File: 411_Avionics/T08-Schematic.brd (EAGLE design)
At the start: 41 parts, among them IC1 BQ24022, J1 USB-MICROB, J3 JST-PH-2-SMT-RA, U3 LSM9DS0, U5 LTC1998, U6 ATMEGA32U4-AU, X1 8MHz

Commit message: Finished board layout!!  Still have to create ground planes and add ground vias, but other than that it's all done.  Hooray!
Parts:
- moved C15 72.5 mm to (11.4, 6.33)
- moved C16 71.7 mm to (9.33, 6.35)
- moved U2 44.5 mm to (16.7, 6.99)
- moved R11 38.6 mm to (32.5, 11.2)
- moved R9 37.7 mm to (32.5, 15.2)
- moved C2 31.9 mm to (48.1, 3.25), turned to 270 degrees
- moved C5 28.2 mm to (48.1, 19.6), turned to 90 degrees
- moved LED1 25.3 mm to (41.1, 22.6), turned to 180 degrees
- moved U3 24.9 mm to (55.0, 18.8)
- moved R10 22.6 mm to (32.5, 13.2)
- moved C13 21.5 mm to (28.5, 19.9)
- moved R7 21.0 mm to (32.3, 22.4), turned to 0 degrees
- moved R6 19.2 mm to (36.8, 22.4), turned to 0 degrees
- moved C3 19.1 mm to (58.5, 21.9), turned to 270 degrees
- moved C6 18.3 mm to (50.2, 19.6), turned to 90 degrees
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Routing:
- net MOSI: track 0.00 -> 64.3 mm, vias 0 -> 3
- net MISO: track 0.00 -> 52.0 mm, vias 0 -> 3
- net VCC: track 46.5 -> 93.3 mm
- net XM_EN: track 0.00 -> 28.9 mm, vias 0 -> 2
- net GYR_EN: track 0.00 -> 26.7 mm, vias 0 -> 2
- net N$1: track 0.00 -> 21.7 mm, vias 0 -> 2
- net N$17: track 0.00 -> 18.6 mm, vias 0 -> 2
- net N$16: track 0.00 -> 18.4 mm, vias 0 -> 2
- net MEM_EN: track 0.00 -> 15.8 mm, vias 0 -> 2
- net N$19: track 0.00 -> 14.6 mm, vias 0 -> 2
- net RED_LED: track 0.00 -> 11.6 mm
- net N$5: track 7.88 -> 18.6 mm, vias 0 -> 2
- net VBUS1: track 4.59 -> 14.9 mm
- net N$8: track 0.00 -> 7.96 mm
- net GREEN_LED: track 0.00 -> 7.91 mm
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
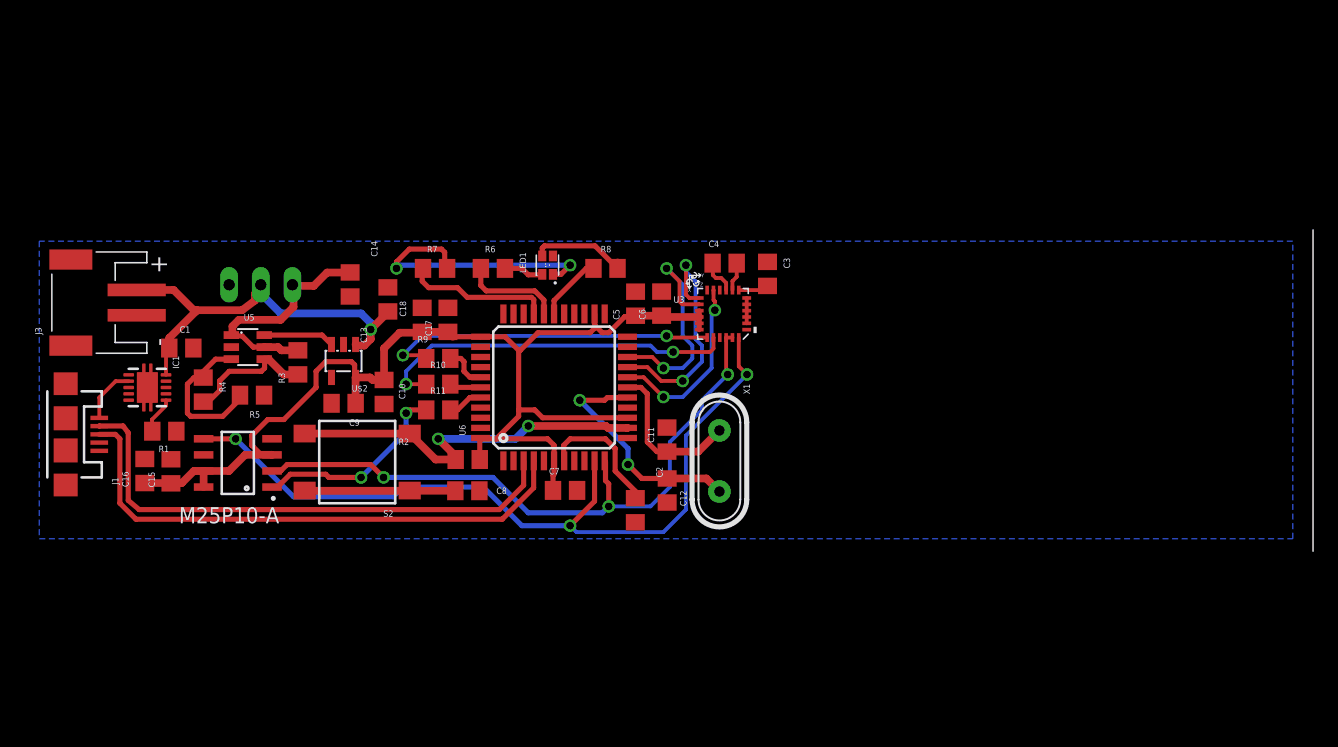
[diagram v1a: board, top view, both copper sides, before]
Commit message: More layout work.  All nodes connected, still need to run through DRC and deal with all that bs.
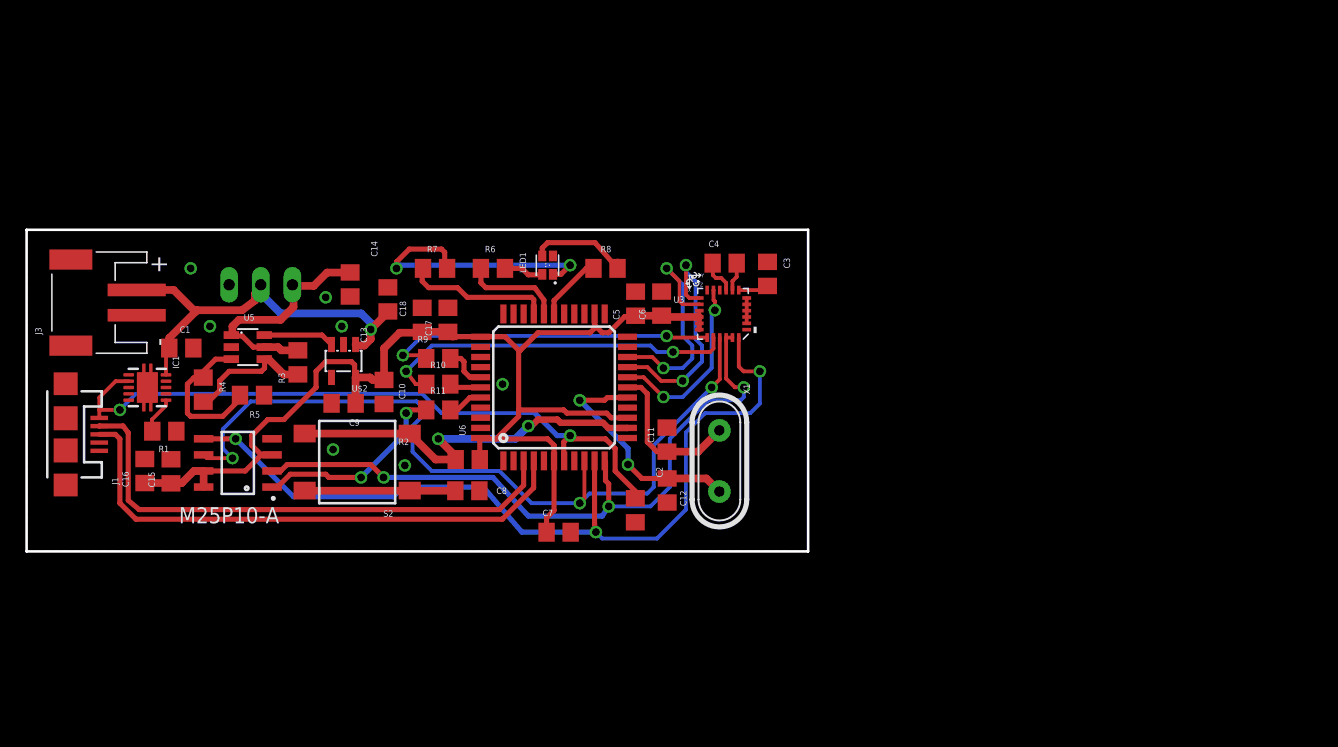
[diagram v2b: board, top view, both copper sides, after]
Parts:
- moved C7 3.34 mm to (42.0, 1.51)
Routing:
- net CLK: track 0.00 -> 64.4 mm, vias 0 -> 3
- net VBUS1: track 14.9 -> 54.3 mm, vias 0 -> 2
- net MOSI: track 64.3 -> 68.3 mm
- net MISO: track 52.0 -> 55.4 mm
- net VCC: track 93.3 -> 95.9 mm
- net XM_EN: track 28.9 -> 28.4 mm
- added copper zone on layer 1, net GND
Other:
- board outline added: 61.7 x 25.4 mm

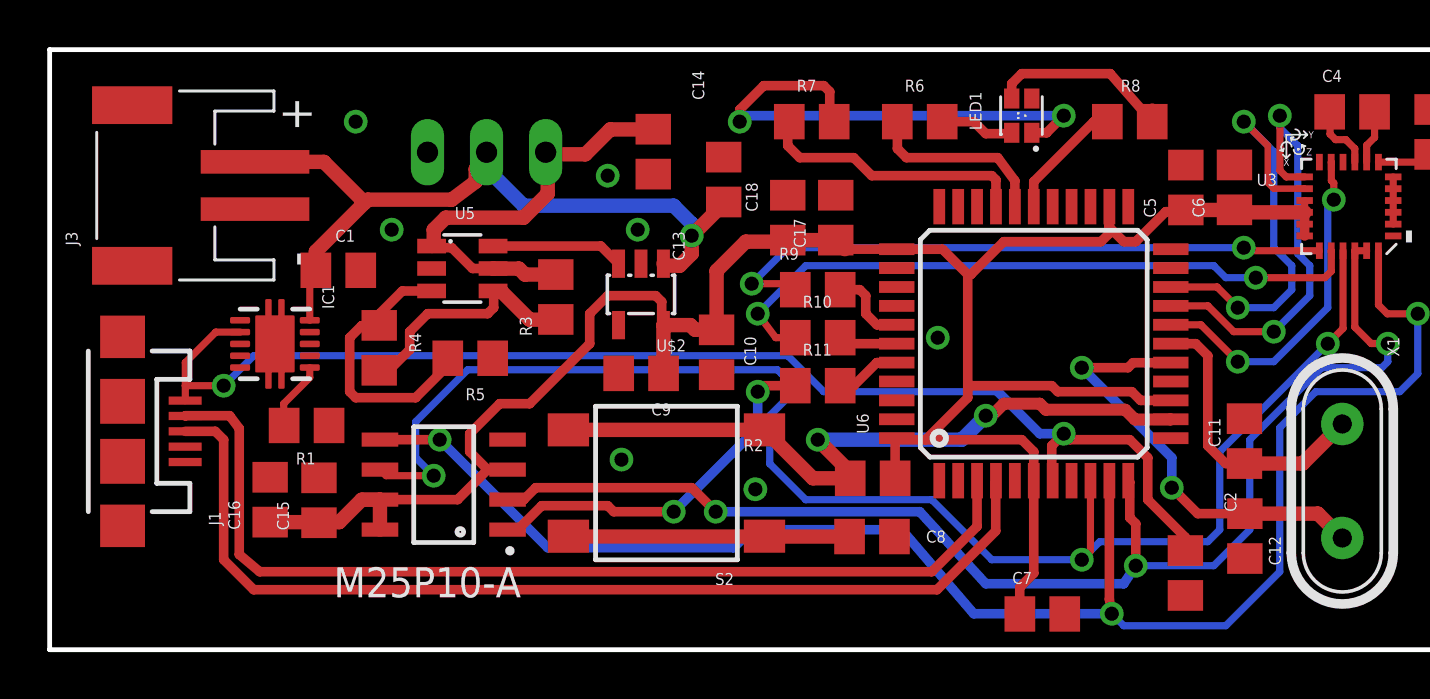
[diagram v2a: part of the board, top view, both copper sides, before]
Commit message: Made some changes to silkscreen layer, fixed package text size.
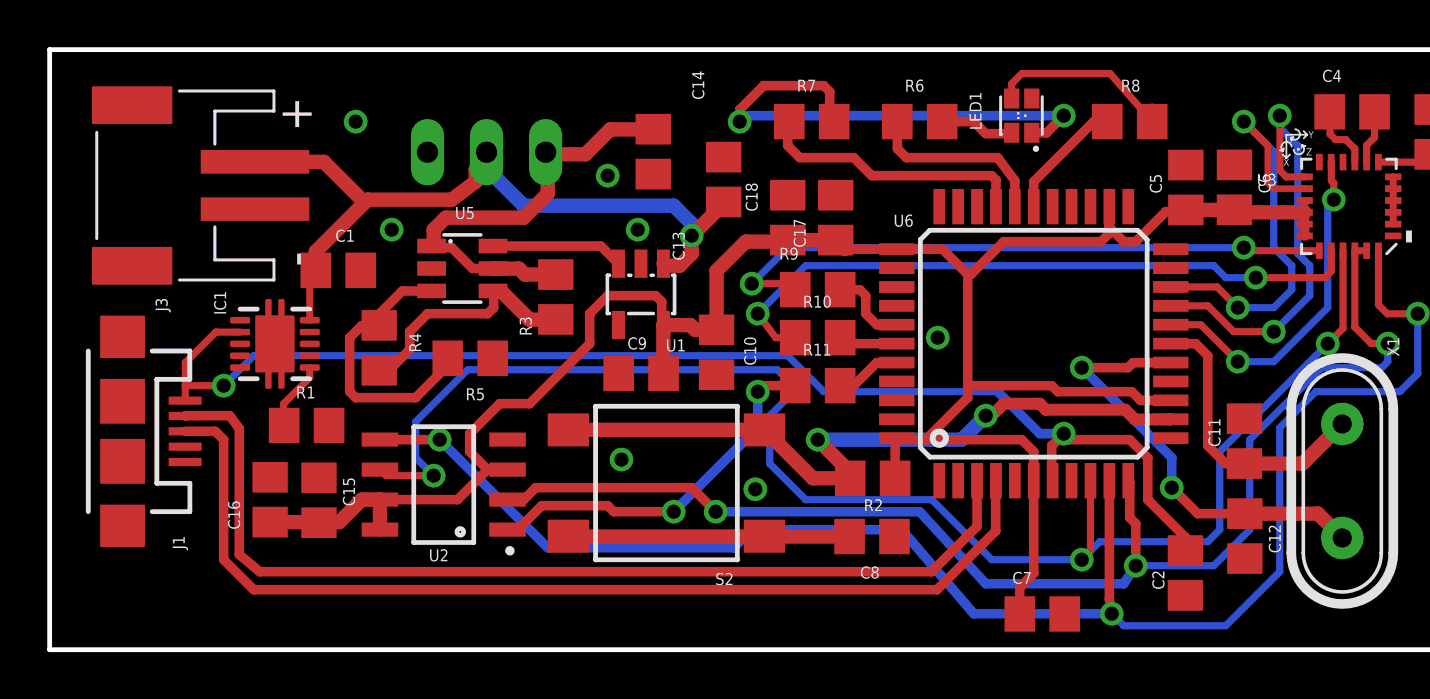
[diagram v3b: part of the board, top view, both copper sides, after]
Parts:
- U2: value (none) -> M25P10-AVMN6TP_TR
- renumbered U$2 to U1

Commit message: Finished preliminary board layout!  Passed OSHParks DRC, hooray!
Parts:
- moved C3 2.19 mm to (58.7, 19.7), turned to 90 degrees
- moved C7 0.64 mm to (41.6, 2.02)
- moved R4 0.51 mm to (14.5, 12.8)
- moved C15 0.51 mm to (11.4, 5.82)
- moved C16 0.51 mm to (9.33, 5.84)
- moved LED1 0.25 mm to (41.1, 22.4)
- moved R1 0.25 mm to (10.9, 9.75)
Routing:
- net GND: track 2.00 -> 6.91 mm, vias 0 -> 31
- net N$1: track 21.7 -> 19.5 mm, vias 2 -> 3
- net VCC: track 95.9 -> 97.1 mm
- net VBUS1: track 54.3 -> 55.3 mm, vias 2 -> 3
- net N$14: track 12.0 -> 11.0 mm
- net MOSI: track 68.3 -> 67.5 mm
- net BLUE_LED: track 5.22 -> 5.97 mm
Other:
- board text added: "Team 8, TinyAV"

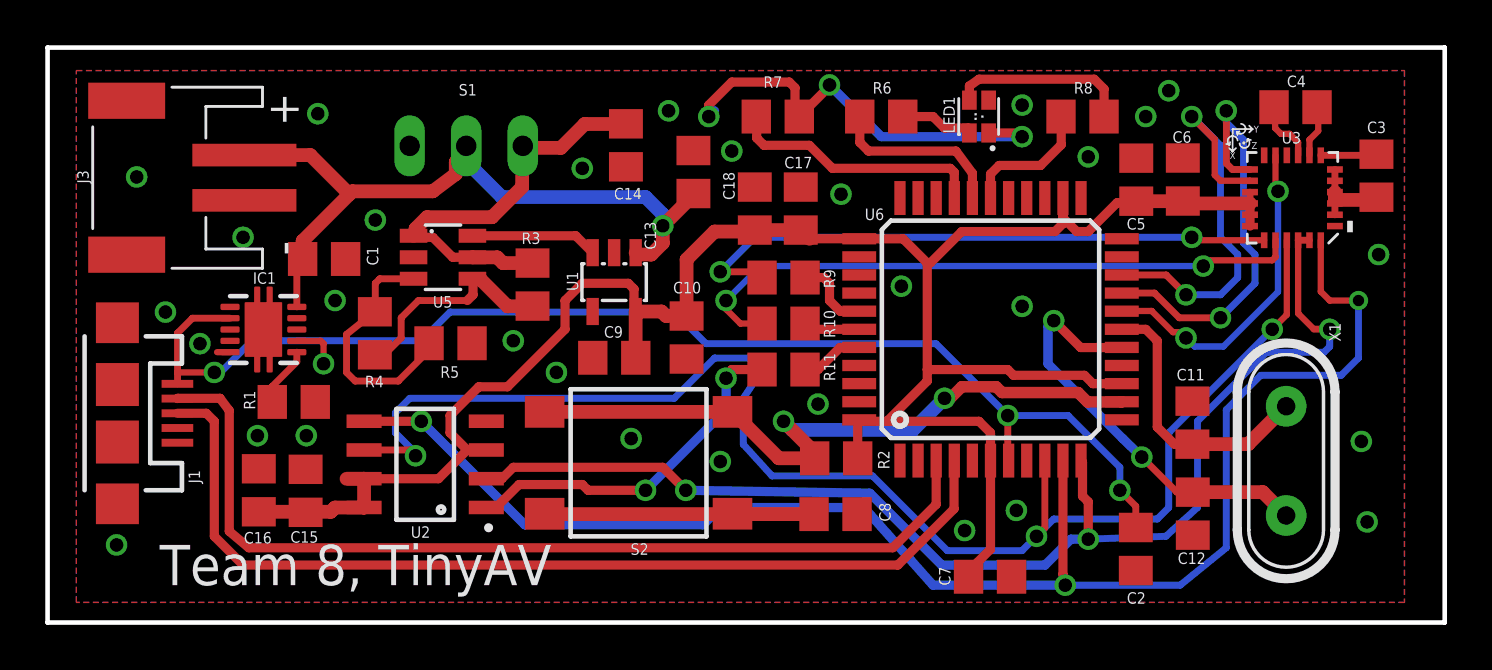
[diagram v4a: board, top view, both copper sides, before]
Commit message: Layout Review #1 With Andrew:
-changed all 0805 packages to 0603  (made a lot more room)
-made vias significantly smaller (made a lot more room)
-updated layout to reflect these changes, no DRC issues

We should consider hooking up the status pins of our battery charger to
LEDs.  Should also consider increasing the value of our current limiting
resistors from the processor.
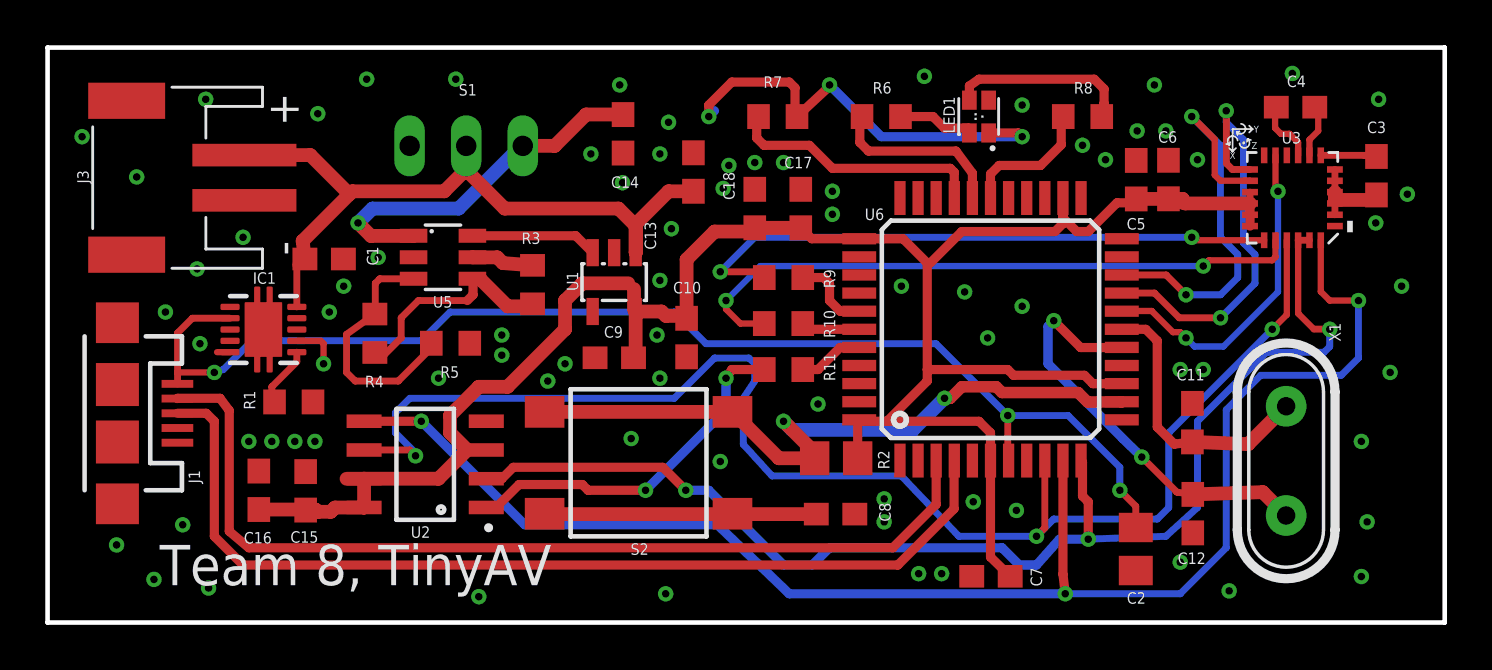
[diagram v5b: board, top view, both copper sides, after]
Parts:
- C1, C10, C11, C12, C13, C14, C15, C16, C17, C18, C3, C4, C5, C6, C7, C8, C9: device rcl:C0805 -> rcl:C0603
- R1, R10, R11, R3, R4, R5, R6, R7, R8, R9: device rcl:R0805 -> rcl:R0603
- moved C6 0.63 mm to (49.5, 19.6)
- moved C14 0.52 mm to (25.4, 21.6)
- turned C7 to 180 degrees
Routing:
- net VCC: track 97.1 -> 99.0 mm
- net MISO: track 55.1 -> 55.9 mm
- net N$15: track 18.4 -> 19.2 mm, vias 0 -> 1
- net N$13: track 32.7 -> 32.2 mm, vias 1 -> 0
- net GND: track 6.91 -> 6.99 mm, vias 31 -> 78
